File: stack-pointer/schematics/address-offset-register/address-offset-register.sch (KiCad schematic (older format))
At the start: 13 parts

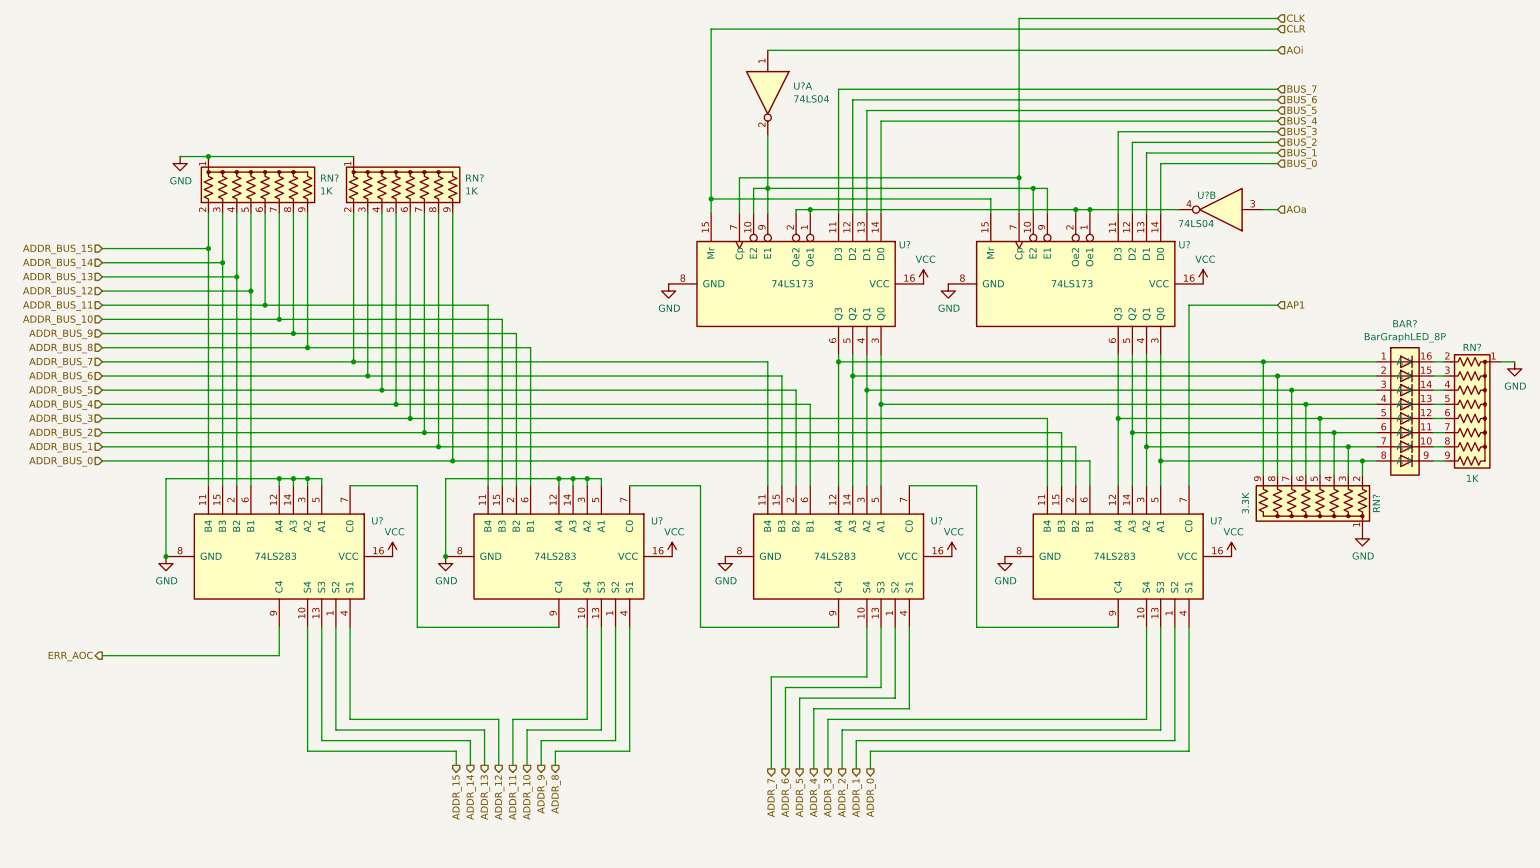
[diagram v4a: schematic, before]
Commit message: added schematics to documentation
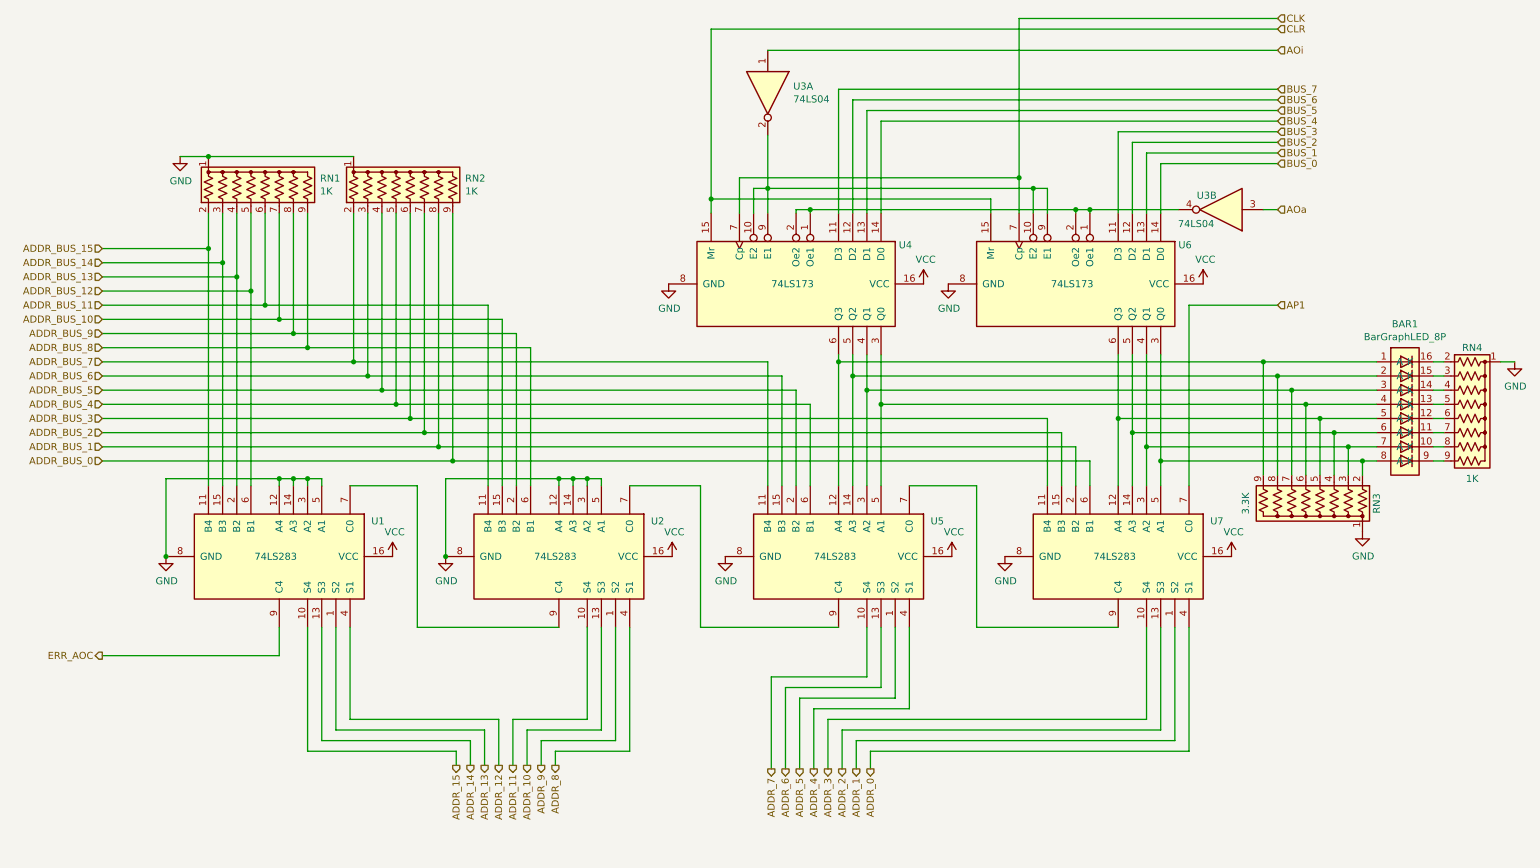
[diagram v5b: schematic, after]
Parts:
- gave numbers to parts that had none: 12
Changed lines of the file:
@@
 Rev ""
 Comp ""
-Comment1 ""
-Comment2 ""
-Comment3 ""
+Comment1 "AOi - read value from data bus into address offset register"
+Comment2 "AOa - write address offset value to address bus adders"
+Comment3 "AP1 - Write a 1 value to carry in of address adders"
 Comment4 ""
 $EndDescr
 $Comp
-L 74xx:74LS283 U?
+L 74xx:74LS283 U7
 U 1 1 61554D20
 P 8325 4650
-F 0 "U?" V 8075 5300 50  0000 L CNN
+F 0 "U7" V 8075 5300 50  0000 L CNN
 F 1 "74LS283" V 8325 4475 50  0000 L CNN
 F 2 "" H 8325 4650 50  0001 C CNN
@@
 $EndComp
 $Comp
-L 74xx:74LS283 U?
+L 74xx:74LS283 U5
 U 1 1 6155A0A2
 P 6350 4650
-F 0 "U?" V 6100 5300 50  0000 L CNN
+F 0 "U5" V 6100 5300 50  0000 L CNN
 F 1 "74LS283" V 6350 4475 50  0000 L CNN
 F 2 "" H 6350 4650 50  0001 C CNN
@@
 $EndComp
 $Comp
-L 74xx:74LS283 U?
+L 74xx:74LS283 U2
 U 1 1 61567DA8
 P 4375 4650
-F 0 "U?" V 4125 5300 50  0000 L CNN
+F 0 "U2" V 4125 5300 50  0000 L CNN
 F 1 "74LS283" V 4375 4475 50  0000 L CNN
 F 2 "" H 4375 4650 50  0001 C CNN
@@
 $EndComp
 $Comp
-L 74xx:74LS283 U?
+L 74xx:74LS283 U1
 U 1 1 61567DAE
 P 2400 4650
-F 0 "U?" V 2150 5300 50  0000 L CNN
+F 0 "U1" V 2150 5300 50  0000 L CNN
 F 1 "74LS283" V 2400 4475 50  0000 L CNN
 F 2 "" H 2400 4650 50  0001 C CNN
@@
 $EndComp
 $Comp
-L 74xx:74LS173 U?
+L 74xx:74LS173 U6
 U 1 1 615718BA
 P 8025 2725
-F 0 "U?" V 7750 3450 50  0000 L CNN
+F 0 "U6" V 7750 3450 50  0000 L CNN
 F 1 "74LS173" V 8025 2550 50  0000 L CNN
 F 2 "" H 8025 2725 50  0001 C CNN
@@
 $EndComp
 $Comp
-L 74xx:74LS173 U?
+L 74xx:74LS173 U4
 U 1 1 61576EAB
 P 6050 2725
-F 0 "U?" V 5775 3450 50  0000 L CNN
+F 0 "U4" V 5775 3450 50  0000 L CNN
 F 1 "74LS173" V 6050 2550 50  0000 L CNN
 F 2 "" H 6050 2725 50  0001 C CNN
@@
 Connection ~ 2400 4100
 $Comp
-L power:GND #PWR?
+L power:GND #PWR04
 U 1 1 615D45E1
 P 3575 4650
-F 0 "#PWR?" H 3575 4400 50  0001 C CNN
+F 0 "#PWR04" H 3575 4400 50  0001 C CNN
 F 1 "GND" H 3580 4477 50  0000 C CNN
 F 2 "" H 3575 4650 50  0001 C CNN
@@
 Connection ~ 3575 4650
 $Comp
-L power:GND #PWR?
+L power:GND #PWR01
 U 1 1 615D4852
 P 1600 4650
-F 0 "#PWR?" H 1600 4400 50  0001 C CNN
+F 0 "#PWR01" H 1600 4400 50  0001 C CNN
 F 1 "GND" H 1605 4477 50  0000 C CNN
 F 2 "" H 1600 4650 50  0001 C CNN
@@
 Connection ~ 1600 4650
 $Comp
-L power:GND #PWR?
+L power:GND #PWR07
 U 1 1 615D4B5E
 P 5550 4650
-F 0 "#PWR?" H 5550 4400 50  0001 C CNN
+F 0 "#PWR07" H 5550 4400 50  0001 C CNN
 F 1 "GND" H 5555 4477 50  0000 C CNN
 F 2 "" H 5550 4650 50  0001 C CNN
@@
 $EndComp
 $Comp
-L power:GND #PWR?
+L power:GND #PWR011
 U 1 1 615D4E0F
 P 7525 4650
-F 0 "#PWR?" H 7525 4400 50  0001 C CNN
+F 0 "#PWR011" H 7525 4400 50  0001 C CNN
 F 1 "GND" H 7530 4477 50  0000 C CNN
 F 2 "" H 7525 4650 50  0001 C CNN
@@
 $EndComp
 $Comp
-L power:GND #PWR?
+L power:GND #PWR09
 U 1 1 615D56CC
 P 7125 2725
-F 0 "#PWR?" H 7125 2475 50  0001 C CNN
+F 0 "#PWR09" H 7125 2475 50  0001 C CNN
 F 1 "GND" H 7130 2552 50  0000 C CNN
 F 2 "" H 7125 2725 50  0001 C CNN
@@
 $EndComp
 $Comp
-L power:GND #PWR?
+L power:GND #PWR05
 U 1 1 615D59EB
 P 5150 2725
-F 0 "#PWR?" H 5150 2475 50  0001 C CNN
+F 0 "#PWR05" H 5150 2475 50  0001 C CNN
 F 1 "GND" H 5155 2552 50  0000 C CNN
 F 2 "" H 5150 2725 50  0001 C CNN
@@
 	6350 3275 6350 3225
 $Comp
-L Device:R_Network08_US RN?
+L Device:R_Network08_US RN4
 U 1 1 615F8167
 P 10825 3675
-F 0 "RN?" V 10325 3675 50  0000 C CNN
+F 0 "RN4" V 10325 3675 50  0000 C CNN
 F 1 "1K" V 11250 3675 50  0000 C CNN
 F 2 "Resistor_THT:R_Array_SIP9" V 11300 3675 50  0001 C CNN
@@
 $EndComp
 $Comp
-L power:GND #PWR?
+L power:GND #PWR015
 U 1 1 615FE144
 P 11125 3275
-F 0 "#PWR?" H 11125 3025 50  0001 C CNN
+F 0 "#PWR015" H 11125 3025 50  0001 C CNN
 F 1 "GND" H 11130 3102 50  0000 C CNN
 F 2 "" H 11125 3275 50  0001 C CNN
@@
 	5450 2125 5450 2225
 $Comp
-L 74xx:74LS04 U?
+L 74xx:74LS04 U3
 U 1 1 616B0543
 P 5850 1375
-F 0 "U?" V 5804 1555 50  0000 L CNN
+F 0 "U3" V 5804 1555 50  0000 L CNN
 F 1 "74LS04" V 5895 1555 50  0000 L CNN
 F 2 "" H 5850 1375 50  0001 C CNN
@@
 	8025 2200 8125 2200
 $Comp
-L power:VCC #PWR?
+L power:VCC #PWR08
 U 1 1 617171F4
 P 6950 2725
-F 0 "#PWR?" H 6950 2575 50  0001 C CNN
+F 0 "#PWR08" H 6950 2575 50  0001 C CNN
 F 1 "VCC" H 6965 2898 50  0000 C CNN
 F 2 "" H 6950 2725 50  0001 C CNN
@@
 $EndComp
 $Comp
-L power:VCC #PWR?
+L power:VCC #PWR012
 U 1 1 61717653
 P 8925 2725
-F 0 "#PWR?" H 8925 2575 50  0001 C CNN
+F 0 "#PWR012" H 8925 2575 50  0001 C CNN
 F 1 "VCC" H 8940 2898 50  0000 C CNN
 F 2 "" H 8925 2725 50  0001 C CNN
@@
 $EndComp
 $Comp
-L power:VCC #PWR?
+L power:VCC #PWR03
 U 1 1 61717AF6
 P 3200 4650
-F 0 "#PWR?" H 3200 4500 50  0001 C CNN
+F 0 "#PWR03" H 3200 4500 50  0001 C CNN
 F 1 "VCC" H 3215 4823 50  0000 C CNN
 F 2 "" H 3200 4650 50  0001 C CNN
@@
 $EndComp
 $Comp
-L power:VCC #PWR?
+L power:VCC #PWR06
 U 1 1 61717F75
 P 5175 4650
-F 0 "#PWR?" H 5175 4500 50  0001 C CNN
+F 0 "#PWR06" H 5175 4500 50  0001 C CNN
 F 1 "VCC" H 5190 4823 50  0000 C CNN
 F 2 "" H 5175 4650 50  0001 C CNN
@@
 $EndComp
 $Comp
-L power:VCC #PWR?
+L power:VCC #PWR010
 U 1 1 61718404
 P 7150 4650
-F 0 "#PWR?" H 7150 4500 50  0001 C CNN
+F 0 "#PWR010" H 7150 4500 50  0001 C CNN
 F 1 "VCC" H 7165 4823 50  0000 C CNN
 F 2 "" H 7150 4650 50  0001 C CNN
@@
 $EndComp
 $Comp
-L power:VCC #PWR?
+L power:VCC #PWR013
 U 1 1 617188A3
 P 9125 4650
-F 0 "#PWR?" H 9125 4500 50  0001 C CNN
+F 0 "#PWR013" H 9125 4500 50  0001 C CNN
 F 1 "VCC" H 9140 4823 50  0000 C CNN
 F 2 "" H 9125 4650 50  0001 C CNN
@@
 	6550 5150 6550 5500
 $Comp
-L 74xx:74LS04 U?
+L 74xx:74LS04 U3
 U 2 1 617B156B
 P 9050 2200
-F 0 "U?" H 9150 2100 50  0000 C CNN
+F 0 "U3" H 9150 2100 50  0000 C CNN
 F 1 "74LS04" H 9225 2300 50  0000 C CNN
 F 2 "" H 9050 2200 50  0001 C CNN
@@
 	5875 5500 5875 6150
 $Comp
-L power:GND #PWR?
+L power:GND #PWR014
 U 1 1 61603AA0
 P 10050 4475
-F 0 "#PWR?" H 10050 4225 50  0001 C CNN
+F 0 "#PWR014" H 10050 4225 50  0001 C CNN
 F 1 "GND" H 10055 4302 50  0000 C CNN
 F 2 "" H 10050 4475 50  0001 C CNN
@@
 	9350 4075 9350 3275
 $Comp
-L common-symbols:BarGraphLED_8P BAR?
+L common-symbols:BarGraphLED_8P BAR1
 U 1 1 615D5CEB
 P 10350 3675
-F 0 "BAR?" H 10350 4342 50  0000 C CNN
+F 0 "BAR1" H 10350 4342 50  0000 C CNN
 F 1 "BarGraphLED_8P" H 10350 4251 50  0000 C CNN
 F 2 "" H 10350 3675 50  0001 C CNN
@@
 $EndComp
 $Comp
-L Device:R_Network08_US RN?
+L Device:R_Network08_US RN3
 U 1 1 615A0052
 P 9650 4275
-F 0 "RN?" V 9150 4275 50  0000 C CNN
+F 0 "RN3" V 9150 4275 50  0000 C CNN
 F 1 "3.3K" V 10075 4275 50  0000 C CNN
 F 2 "Resistor_THT:R_Array_SIP9" V 10125 4275 50  0001 C CNN
@@
 	8825 2875 8825 4150
 $Comp
-L Device:R_Network08_US RN?
+L Device:R_Network08_US RN1
 U 1 1 6161A5EE
 P 2300 2025
-F 0 "RN?" H 2688 2071 50  0000 L CNN
+F 0 "RN1" H 2688 2071 50  0000 L CNN
 F 1 "1K" H 2688 1980 50  0000 L CNN
 F 2 "Resistor_THT:R_Array_SIP9" V 2775 2025 50  0001 C CNN
@@
 $EndComp
 $Comp
-L Device:R_Network08_US RN?
+L Device:R_Network08_US RN2
 U 1 1 6161C78B
 P 3325 2025
-F 0 "RN?" H 3713 2071 50  0000 L CNN
+F 0 "RN2" H 3713 2071 50  0000 L CNN
 F 1 "1K" H 3713 1980 50  0000 L CNN
 F 2 "Resistor_THT:R_Array_SIP9" V 3800 2025 50  0001 C CNN
@@
 	2925 1825 1900 1825
 $Comp
-L power:GND #PWR?
+L power:GND #PWR02
 U 1 1 6170BD34
 P 1700 1825
-F 0 "#PWR?" H 1700 1575 50  0001 C CNN
+F 0 "#PWR02" H 1700 1575 50  0001 C CNN
 F 1 "GND" H 1705 1652 50  0000 C CNN
 F 2 "" H 1700 1825 50  0001 C CNN
